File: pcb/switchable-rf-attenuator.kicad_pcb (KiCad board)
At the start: 4 copper layers, 48.2 x 30 mm, 17 parts, among them J1 USB_B_Mini, J2 Conn_Coaxial, J3 Conn_Coaxial, SW1 SW_SPDT, U1 AS179-92LF, U2 AS179-92LF

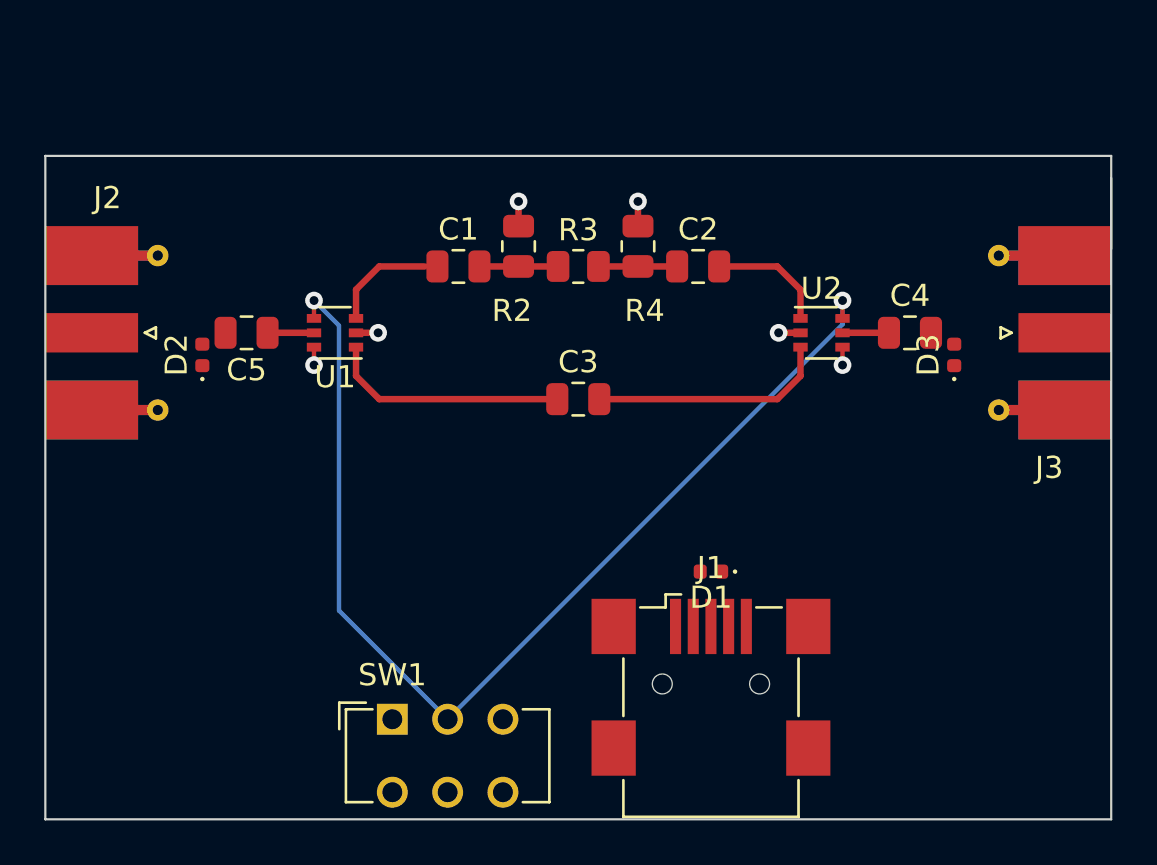
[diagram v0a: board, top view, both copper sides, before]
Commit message: finish the trace routing
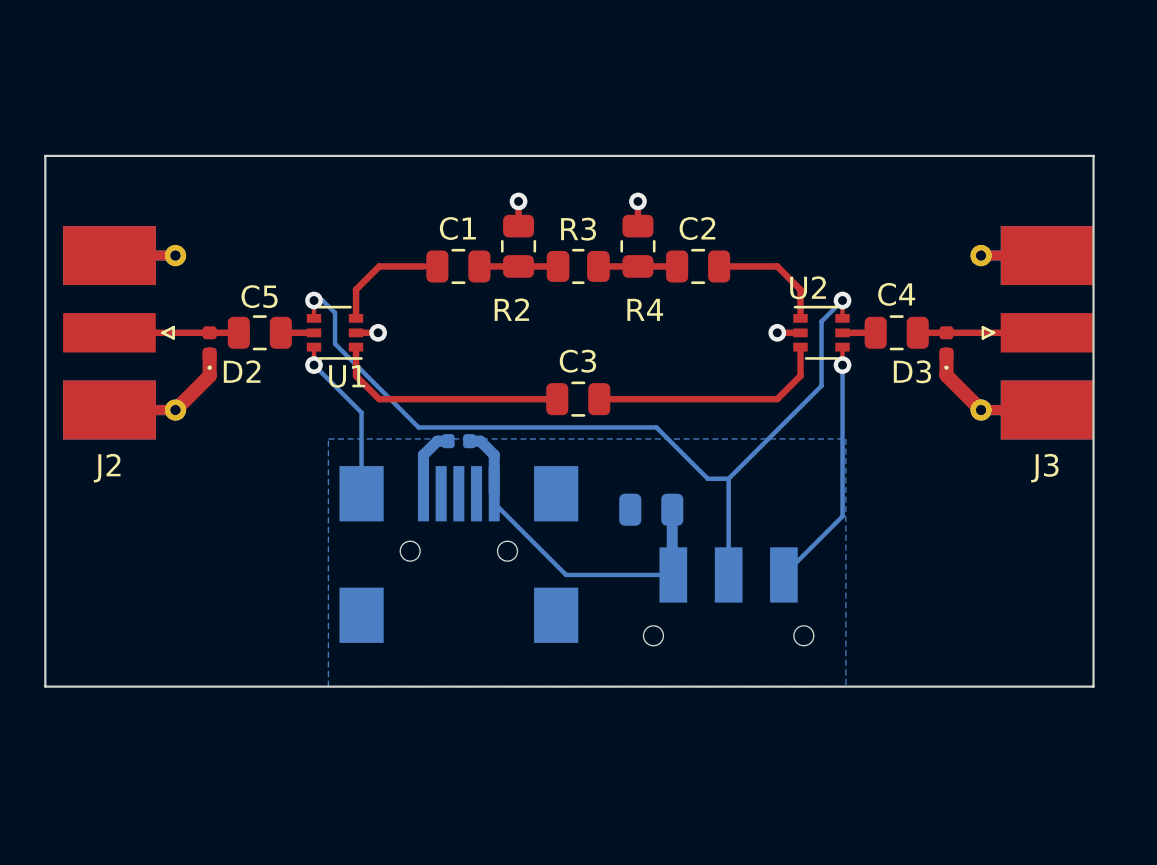
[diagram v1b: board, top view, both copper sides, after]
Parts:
- added C6: 0.1uF, Capacitor_SMD:C_0805_2012Metric, B.Cu at (172.3, 126.0)
- C4, C5: value 33p -> 0.33p
- D1, J1: moved to B.Cu
- SW1: footprint Button_Switch_THT:SW_CuK_JS202011AQN_DPDT_Angled -> Button_Switch_SMD:SW_SPDT_CK-JS102011SAQN; moved to B.Cu
- moved SW1 15.7 mm to (175.8, 131.7), turned to 180 degrees
- moved J1 12.9 mm to (163.6, 127.9), turned to 180 degrees
- moved D1 12.8 mm to (163.6, 122.9), turned to 0 degrees
- moved J2 0.80 mm to (147.8, 118.0)
- moved J3 0.80 mm to (190.2, 118.0)
- moved D3 0.62 mm to (185.7, 118.5)
- moved D2 0.61 mm to (152.3, 118.5)
- moved C4 0.60 mm to (183.4, 118.0)
- moved C5 0.60 mm to (154.6, 118.0)
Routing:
- net GND: track 1.62 -> 22.0 mm
- net +5V: track 0.00 -> 16.0 mm
- net /V_CTL: track 49.4 -> 39.1 mm
- net GNDA: track 4.22 -> 10.6 mm
- net Net-(C5-Pad2): track 0.00 -> 5.85 mm
- net Net-(C4-Pad2): track 0.00 -> 5.85 mm
- net /OUT: track 2.10 -> 1.50 mm
- net /IN: track 2.10 -> 1.50 mm
- added copper zone on B.Cu, net GND
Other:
- board size 48.2 x 30 mm -> 47.4 x 24 mm

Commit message: add a note
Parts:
- added JP1: SolderJumper_2_Open, Jumper:SolderJumper-2_P1.3mm_Open_TrianglePad1.0x1.5mm, B.Cu at (155.7, 124.8)
- added R1: 37.4R, Resistor_SMD:R_0805_2012Metric, B.Cu at (176.7, 126.0)
- C1, C2, C3: value 33p -> NC
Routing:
- net GNDA: track 10.6 -> 16.1 mm
- net GND: track 22.0 -> 25.0 mm
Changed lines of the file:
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@@
       (effects (font (size 1 1) (thickness 0.15)))
     )
-    (fp_text value "33p" (at 0 1.68) (layer "F.Fab") hide
+    (fp_text value "NC" (at 0 1.68) (layer "F.Fab") hide
       (effects (font (size 1 1) (thickness 0.15)))
     )
@@
       (effects (font (size 1 1) (thickness 0.15)))
     )
-    (fp_text value "33p" (at 0 1.68) (layer "F.Fab") hide
+    (fp_text value "NC" (at 0 1.68) (layer "F.Fab") hide
       (effects (font (size 1 1) (thickness 0.15)))
     )
@@
       (effects (font (size 1 1) (thickness 0.15)))
     )
-    (fp_text value "33p" (at 0 1.68) (layer "F.Fab") hide
+    (fp_text value "NC" (at 0 1.68) (layer "F.Fab") hide
       (effects (font (size 1 1) (thickness 0.15)))
     )
@@
     (property "Sheetname" "")
     (attr smd)
-    (fp_text reference "SW1" (at 6.6 -1.4) (layer "B.SilkS")
+    (fp_text reference "SW1" (at -6.5 -1.4) (layer "B.SilkS")
       (effects (font (size 1 1) (thickness 0.15)) (justify mirror))
     )
@@
     )
   )
+  (footprint "Jumper:SolderJumper-2_P1.3mm_Open_TrianglePad1.0x1.5mm" (layer "B.Cu")
+    (at 155.7 124.8 180)
+    (descr "SMD Solder Jumper, 1x1.5mm Triangular Pads, 0.3mm gap, open")
+    (tags "solder jumper open")
+    (property "Sheetfile" "switchable-rf-attenuator.kicad_sch")
+    (property "Sheetname" "")
+    (attr exclude_from_pos_files)
+    (fp_text reference "JP1" (at 0 1.8) (layer "B.SilkS")
+      (effects (font (size 1 1) (thickness 0.15)) (justify mirror))
+    )
+    (fp_text value "SolderJumper_2_Open" (at 0 -1.9) (layer "B.Fab") hide
+      (effects (font (size 1 1) (thickness 0.15)) (justify mirror))
+    )
+    (fp_line (start -1.4 -1) (end -1.4 1) (layer "B.SilkS") (width 0.12))
+    (fp_line (start 1.4 1) (end 1.4 -1) (layer "B.SilkS") (width 0.12))
+    (fp_line (start -1.4 1) (end 1.4 1) (layer "B.SilkS") (width 0.12))
+    (fp_line (start 1.4 -1) (end -1.4 -1) (layer "B.SilkS") (width 0.12))
+    (fp_line (start 1.65 -1.25) (end -1.65 -1.25) (layer "B.CrtYd") (width 0.05))
+    (fp_line (start -1.65 1.25) (end -1.65 -1.25) (layer "B.CrtYd") (width 0.05))
+    (fp_line (start 1.65 -1.25) (end 1.65 1.25) (layer "B.CrtYd") (width 0.05))
+    (fp_line (start -1.65 1.25) (end 1.65 1.25) (layer "B.CrtYd") (width 0.05))
+    (pad "1" smd custom (at -0.725 0 180) (size 0.3 0.3) (layers "B.Cu" "B.Mask")
+      (net 1 "GND") (pinfunction "A") (pintype "passive") (zone_connect 2)
+      (options (clearance outline) (anchor rect))
+      (primitives
+        (gr_poly (pts
+            (xy 1 0)
+            (xy 0.5 -0.75)
+            (xy -0.5 -0.75)
+            (xy -0.5 0.75)
+            (xy 0.5 0.75)
+          ) (width 0) (fill yes))
+      ))
+    (pad "2" smd custom (at 0.725 0 180) (size 0.3 0.3) (layers "B.Cu" "B.Mask")
+      (net 11 "GNDA") (pinfunction "B") (pintype "passive") (zone_connect 2)
+      (options (clearance outline) (anchor rect))
+      (primitives
+        (gr_poly (pts
+            (xy 0.5 -0.75)
+            (xy -0.65 -0.75)
+            (xy -0.15 0)
+            (xy -0.65 0.75)
+            (xy 0.5 0.75)
+          ) (width 0) (fill yes))
+      ))
+  )
+  (footprint "Resistor_SMD:R_0805_2012Metric" (layer "B.Cu")
+    (at 176.6875 126 180)
+    (descr "Resistor SMD 0805 (2012 Metric), square (rectangular) end terminal, IPC_7351 nominal, (Body size source: IPC-SM-782 page 72, https://www.pcb-3d.com/wordpress/wp-content/uploads/ipc-sm-782a_amendment_1_and_2.pdf), generated with kicad-footprint-generator")
+    (tags "resistor")
+    (property "Sheetfile" "switchable-rf-attenuator.kicad_sch")
+    (property "Sheetname" "")
+    (attr smd)
+    (fp_text reference "R1" (at 0 1.65) (layer "B.SilkS")
+      (effects (font (size 1 1) (thickness 0.15)) (justify mirror))
+    )
+    (fp_text value "37.4R" (at 0 -1.65) (layer "B.Fab") hide
+      (effects (font (size 1 1) (thickness 0.15)) (justify mirror))
+    )
+    (fp_text user "${REFERENCE}" (at 0 0) (layer "B.Fab")
+      (effects (font (size 0.5 0.5) (thickness 0.08)) (justify mirror))
+    )
+    (fp_line (start -0.227064 -0.735) (end 0.227064 -0.735) (layer "B.SilkS") (width 0.12))
+    (fp_line (start -0.227064 0.735) (end 0.227064 0.735) (layer "B.SilkS") (width 0.12))
+    (fp_line (start -1.68 -0.95) (end -1.68 0.95) (layer "B.CrtYd") (width 0.05))
+    (fp_line (start 1.68 -0.95) (end -1.68 -0.95) (layer "B.CrtYd") (width 0.05))
+    (fp_line (start -1.68 0.95) (end 1.68 0.95) (layer "B.CrtYd") (width 0.05))
+    (fp_line (start 1.68 0.95) (end 1.68 -0.95) (layer "B.CrtYd") (width 0.05))
+    (fp_line (start -1 -0.625) (end -1 0.625) (layer "B.Fab") (width 0.1))
+    (fp_line (start 1 -0.625) (end -1 -0.625) (layer "B.Fab") (width 0.1))
+    (fp_line (start -1 0.625) (end 1 0.625) (layer "B.Fab") (width 0.1))
+    (fp_line (start 1 0.625) (end 1 -0.625) (layer "B.Fab") (width 0.1))
+    (pad "1" smd roundrect (at -0.9125 0 180) (size 1.025 1.4) (layers "B.Cu" "B.Paste" "B.Mask") (roundrect_rratio 0.243902)
+      (net 1 "GND") (pintype "passive"))
+    (pad "2" smd roundrect (at 0.9125 0 180) (size 1.025 1.4) (layers "B.Cu" "B.Paste" "B.Mask") (roundrect_rratio 0.243902)
+      (net 3 "/V_CTL") (pintype "passive"))
+    (model "${KICAD6_3DMODEL_DIR}/Resistor_SMD.3dshapes/R_0805_2012Metric.wrl"
+      (offset (xyz 0 0 0))
+      (scale (xyz 1 1 1))
+      (rotate (xyz 0 0 0))
+    )
+  )
   (footprint "Capacitor_SMD:C_0805_2012Metric" (layer "B.Cu")
     (at 172.3 126 180)
@@
     (property "Sheetname" "")
     (attr smd)
-    (fp_text reference "J1" (at -6.8 -4.015) (layer "B.SilkS")
+    (fp_text reference "J1" (at -5.1 -5.225) (layer "B.SilkS")
       (effects (font (size 1 1) (thickness 0.15)) (justify mirror))
     )
@@
   (segment (start 162 125.275) (end 162 123.525) (width 0.5) (layer "B.Cu") (net 1))
   (segment (start 157.05 119.46) (end 159.2 121.61) (width 0.2) (layer "B.Cu") (net 1))
+  (segment (start 156.425 124.8) (end 158.725 124.8) (width 0.5) (layer "B.Cu") (net 1))
+  (segment (start 158.725 124.8) (end 159.2 125.275) (width 0.5) (layer "B.Cu") (net 1))
   (segment (start 159.2 121.61) (end 159.2 125.275) (width 0.2) (layer "B.Cu") (net 1))
   (segment (start 180.95 126.3) (end 180.95 119.46) (width 0.2) (layer "B.Cu") (net 1))
@@
   (via (at 178 118) (size 0.8) (drill 0.4) (layers "F.Cu" "B.Cu") (net 11))
   (via (at 159.95 118) (size 0.8) (drill 0.4) (layers "F.Cu" "B.Cu") (net 11))
+  (segment (start 154.975 124.8) (end 154.0925 124.8) (width 0.5) (layer "B.Cu") (net 11))
+  (segment (start 154.0925 124.8) (end 150.785 121.4925) (width 0.5) (layer "B.Cu") (net 11))
   (segment (start 168.0875 115) (end 164.53 115) (width 0.29337) (layer "F.Cu") (net 12))
   (segment (start 169.9125 115) (end 173.47 115) (width 0.29337) (layer "F.Cu") (net 13))

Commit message: add assets
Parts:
- added H1: MountingHole_Pad, MountingHole:MountingHole_2.2mm_M2_Pad_Via, F.Cu at (148.0, 130.9)
- added H2: MountingHole_Pad, MountingHole:MountingHole_2.2mm_M2_Pad_Via, F.Cu at (148.0, 108.1)
- added H3: MountingHole_Pad, MountingHole:MountingHole_2.2mm_M2_Pad_Via, F.Cu at (189.2, 130.9)
- added H4: MountingHole_Pad, MountingHole:MountingHole_2.2mm_M2_Pad_Via, F.Cu at (189.2, 108.1)
- U1, U2: value AS179-92LF -> AS183-73LF
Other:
- board size 47.4 x 24 mm -> 47.4 x 29 mm

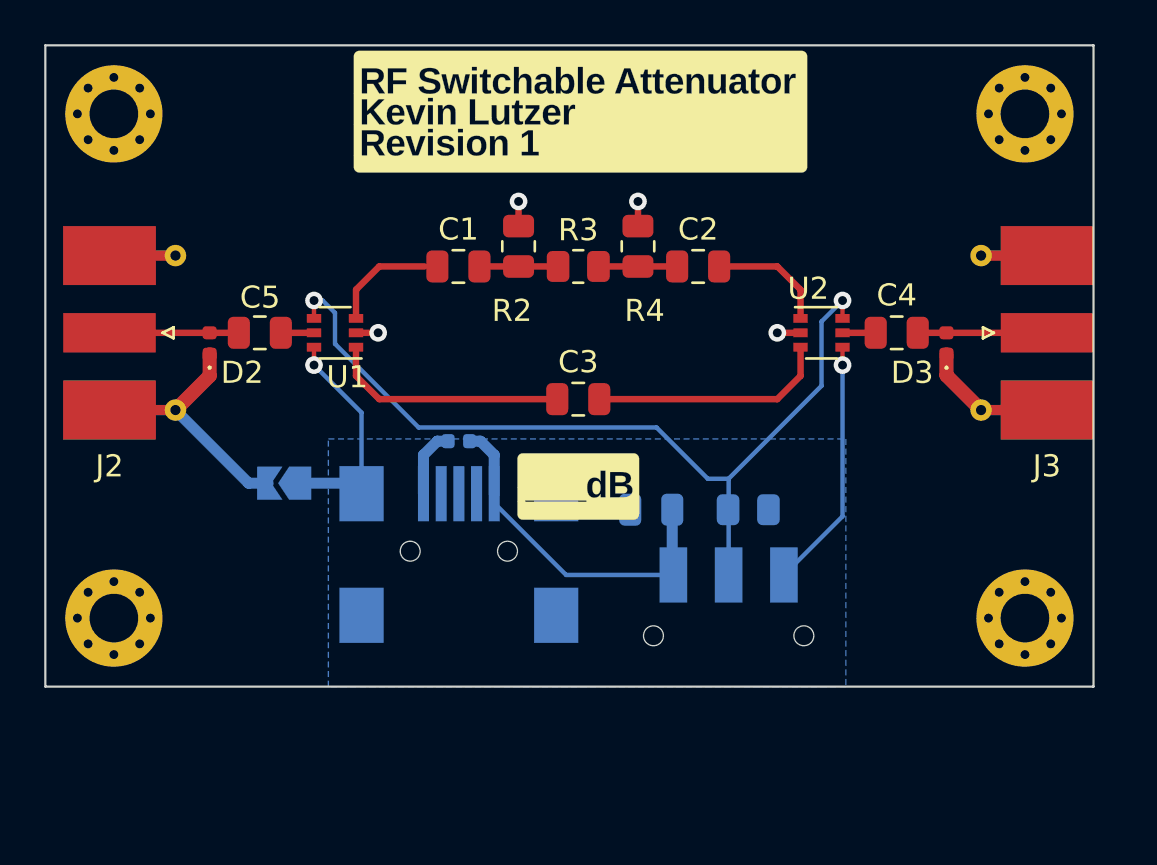
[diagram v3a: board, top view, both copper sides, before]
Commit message: round corners, add stitching vias and via fence around tl
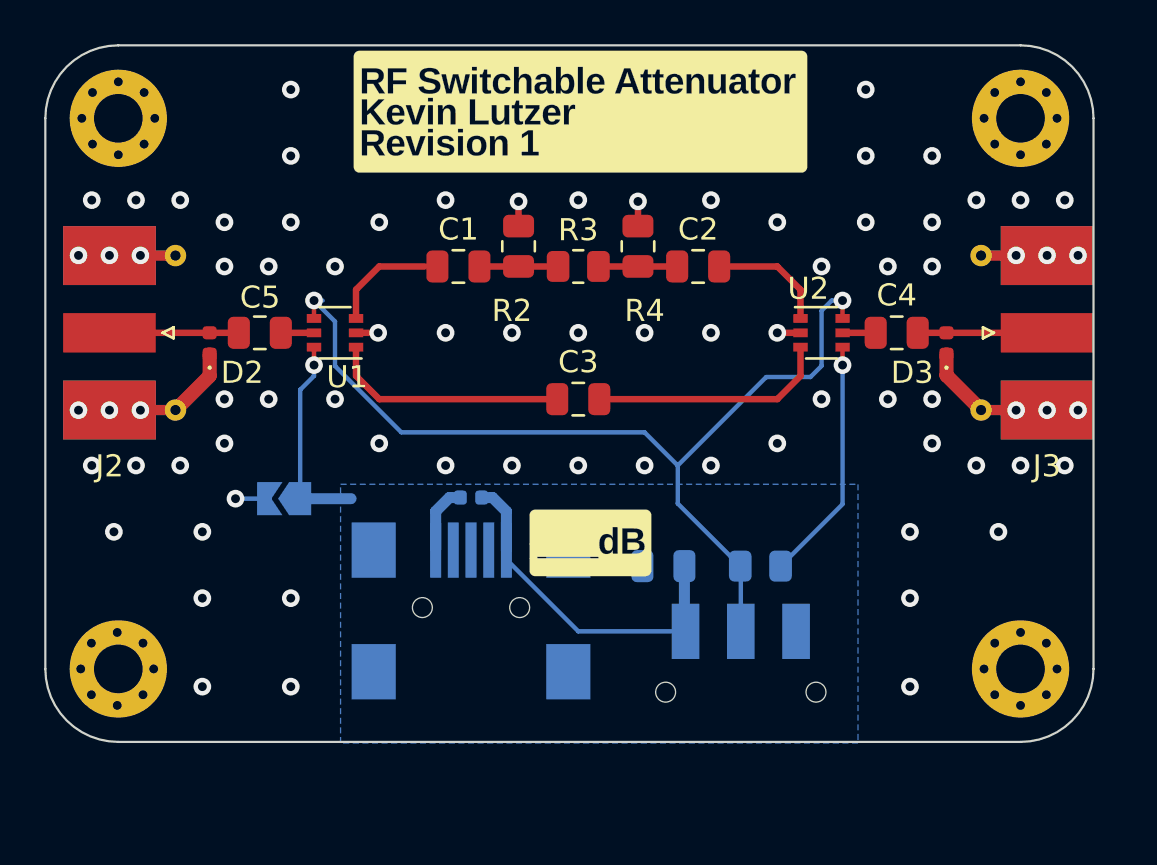
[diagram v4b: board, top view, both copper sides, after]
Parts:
- moved J1 2.61 mm to (164.2, 130.4)
- moved R1 2.61 mm to (177.2, 128.6)
- moved C6 2.61 mm to (172.8, 128.6)
- moved SW1 2.61 mm to (176.3, 134.2)
- moved D1 2.61 mm to (164.2, 125.5)
- moved H3 2.31 mm to (189.0, 133.2)
- moved H1 2.30 mm to (148.2, 133.2)
- moved JP1 0.70 mm to (155.7, 125.5)
- moved H2 0.28 mm to (148.2, 108.3)
- moved H4 0.28 mm to (189.0, 108.3)
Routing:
- net /V_CTL: track 39.1 -> 43.4 mm
- net GNDA: track 16.1 -> 12.0 mm, vias 4 -> 79
- net GND: track 25.0 -> 24.3 mm
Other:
- board size 47.4 x 29 mm -> 47.4 x 31.5 mm

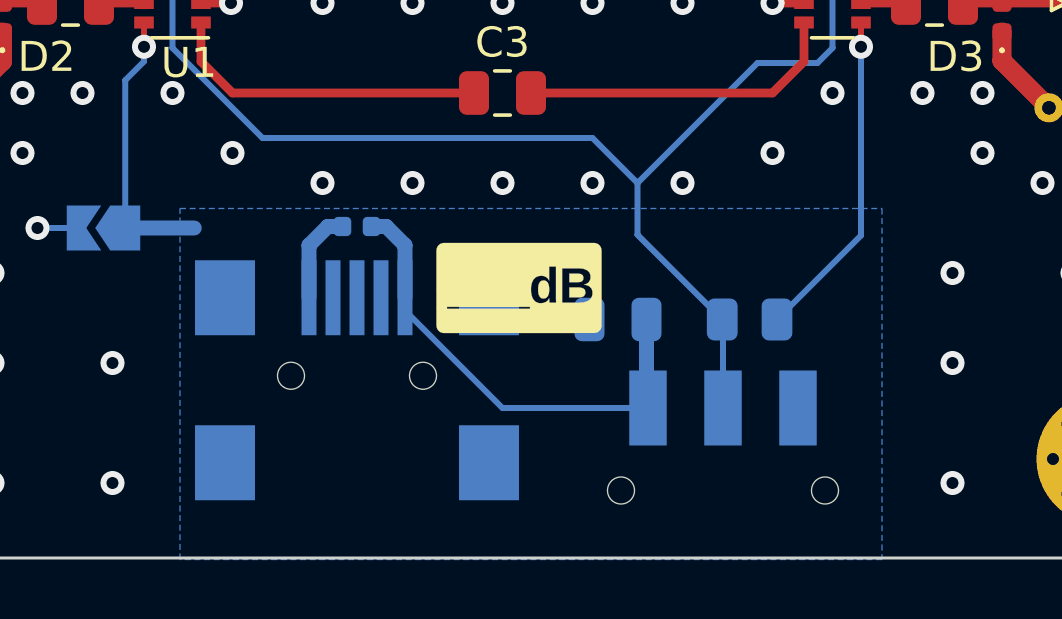
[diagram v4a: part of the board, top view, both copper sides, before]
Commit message: add bom and add a LPF for the DC signals
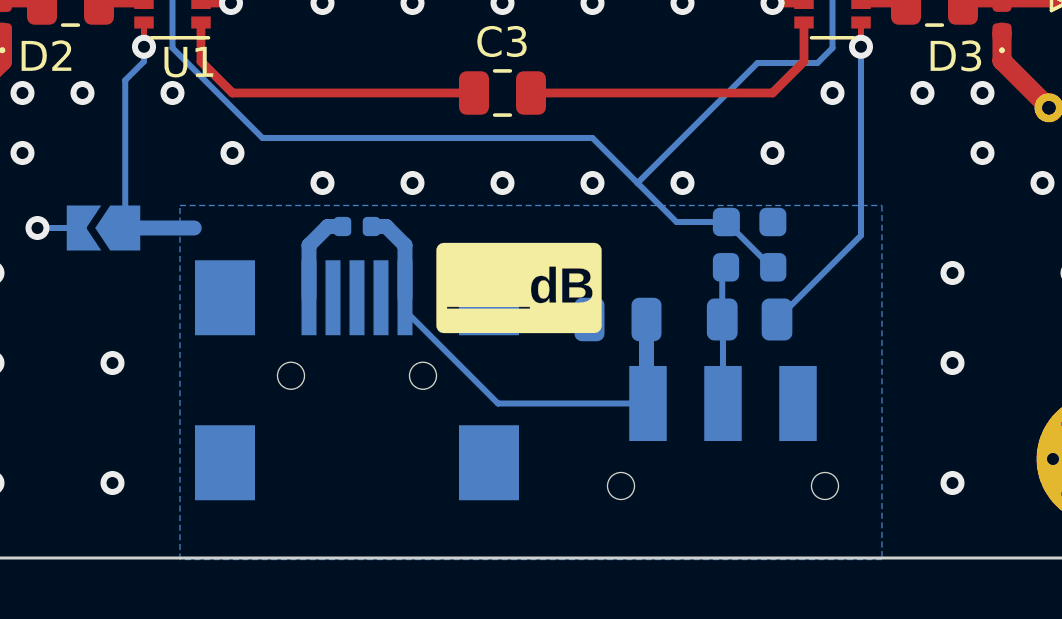
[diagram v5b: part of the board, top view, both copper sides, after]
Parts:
- added C7: 100nF, Capacitor_SMD:C_0603_1608Metric, B.Cu at (177.2, 125.3)
- added FB1: FerriteBead_Small, Inductor_SMD:L_0603_1608Metric, B.Cu at (177.2, 126.8)
- D2, D3: value LXES15AAA1-100 -> ESD110B102ELE6327XTMA1
- moved SW1 0.15 mm to (176.3, 134.1)
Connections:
- R1 pad 2: /V_CTL -> /V_SW
- SW1 pad 2: /V_CTL -> /V_SW
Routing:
- net /V_SW: track 0.00 -> 4.60 mm
- net /V_CTL: track 43.4 -> 40.4 mm
